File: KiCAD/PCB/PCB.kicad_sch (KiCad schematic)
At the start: 62 parts, among them J1 Conn_01x04, J2 Conn_01x02, P1 USB_C_Plug, Q1 Q_NPN_EBC, Q2 Q_NPN_EBC, SW1 SW_Push, SW2 SW_Push, SW3 RotaryEncoder_Switch, SW4 SW_Push, SW5 SW_Push, U1 MIC5219-3.3YM5, U2 CH340G, U3 MCP73832-5-OT, U4 ESP32-WROOM-32D, U5 MPU-6050, Y1 12Mhz

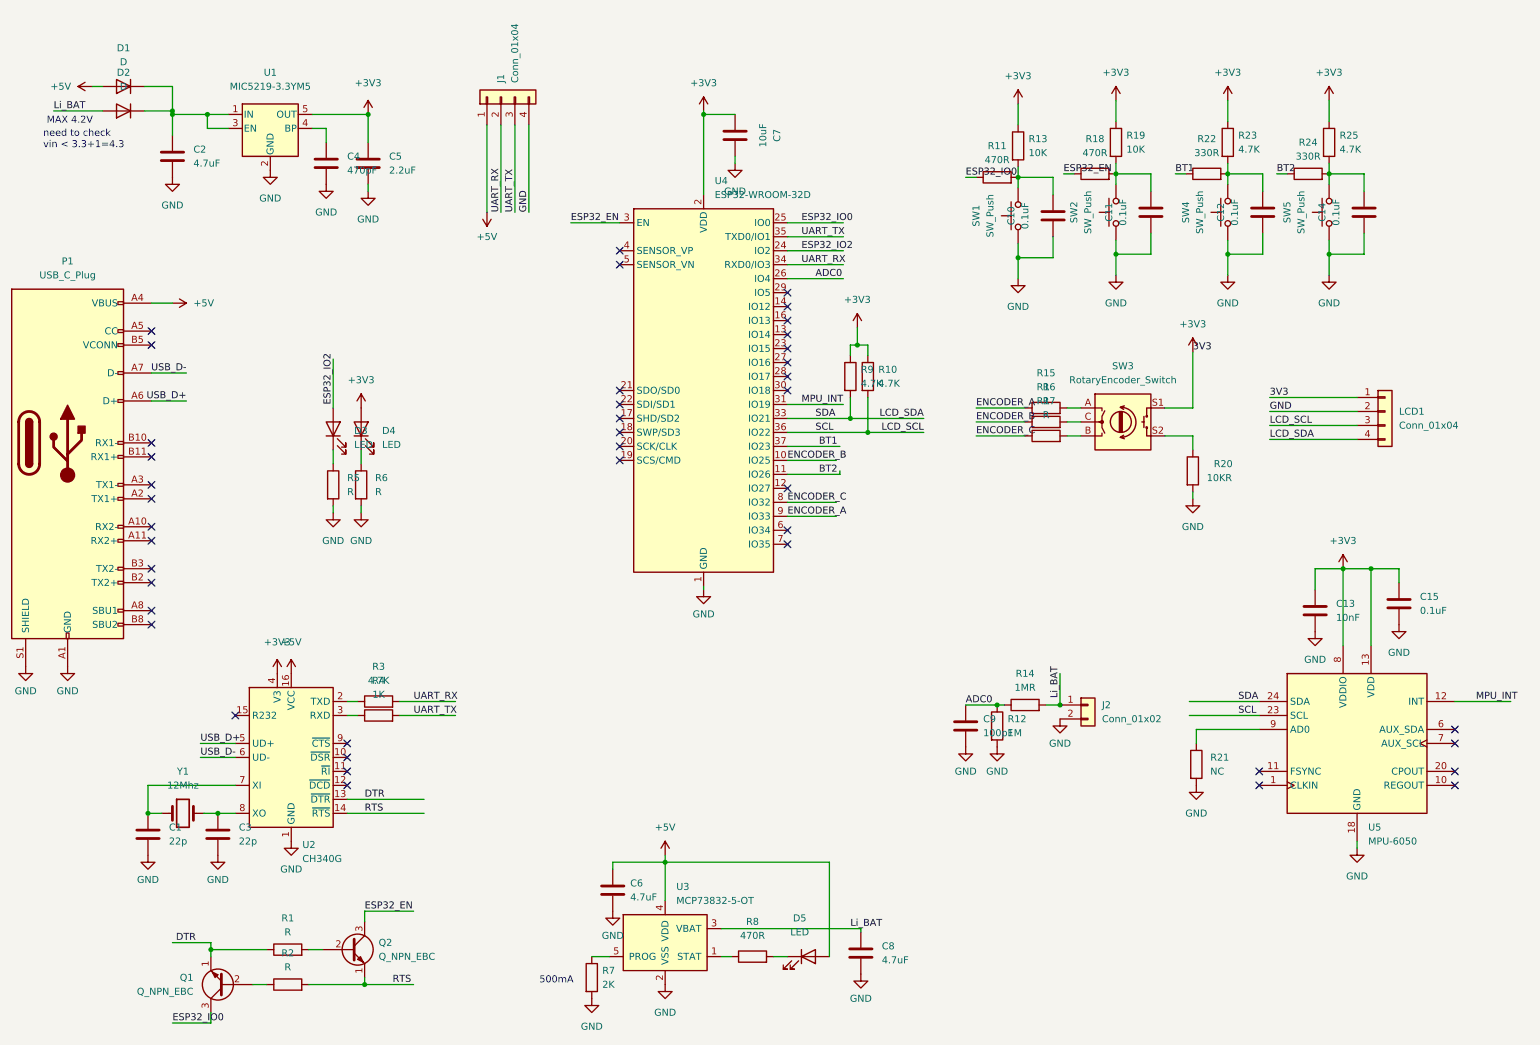
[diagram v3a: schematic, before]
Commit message: 更新第二版原理圖
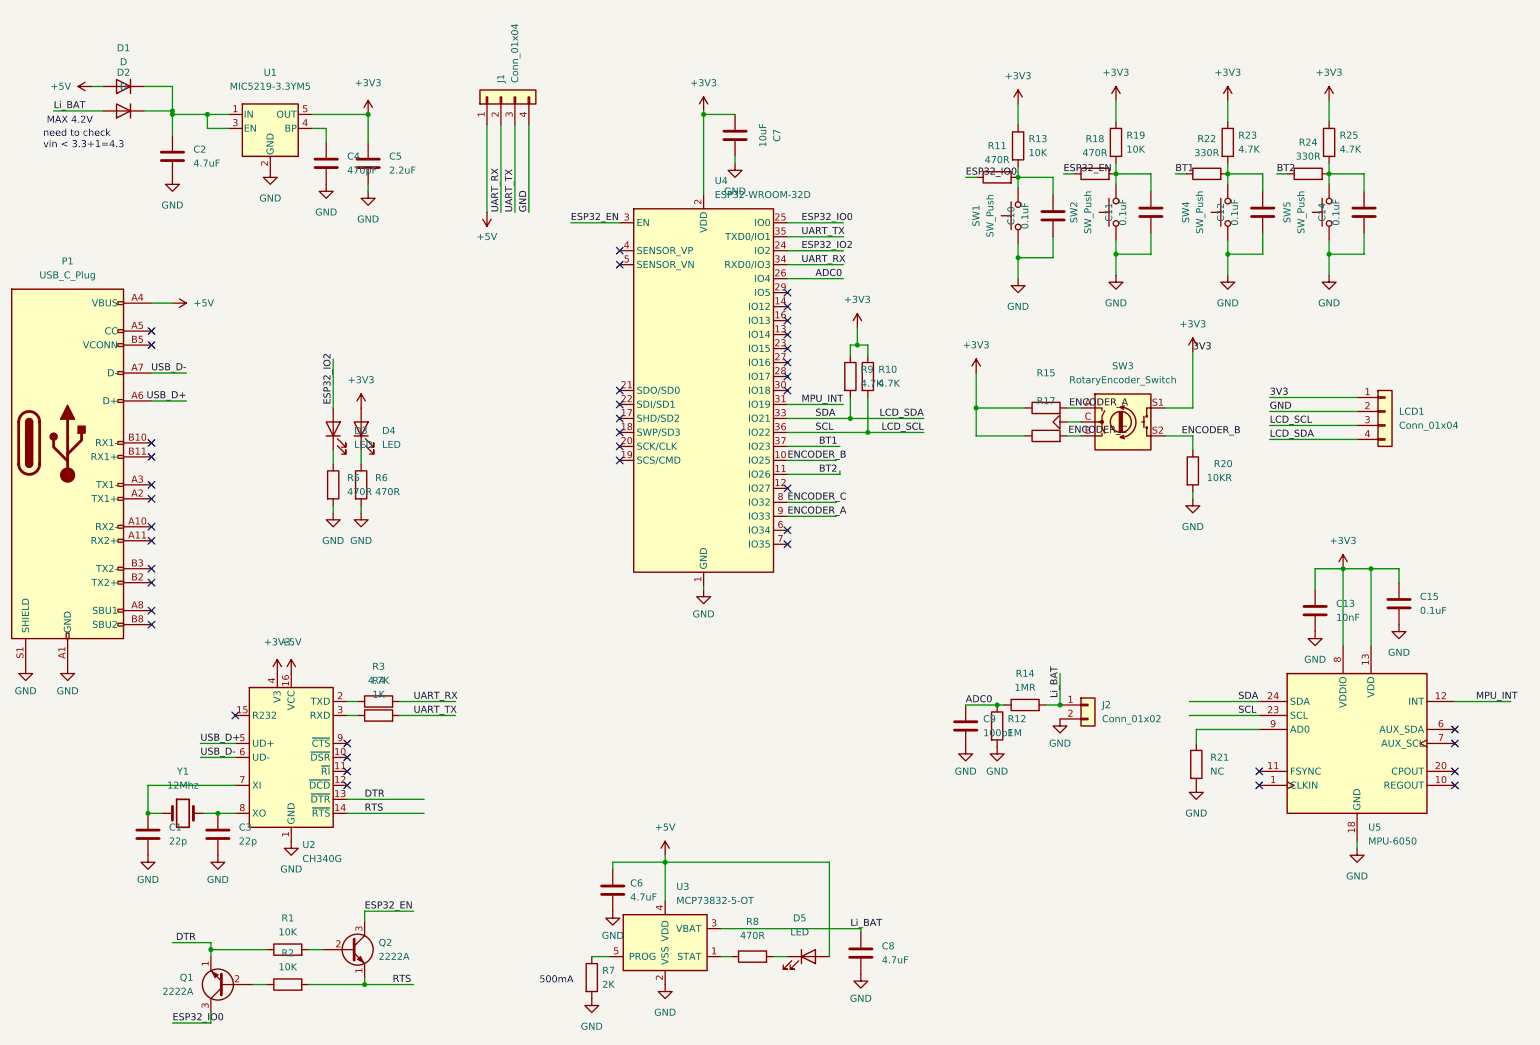
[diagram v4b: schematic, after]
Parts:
- removed R16: R, Resistor_SMD:R_0402_1005Metric, symbol Device:R
- Q1, Q2: value Q_NPN_EBC -> 2222A
- R1, R2: value R -> 10K
- R15, R17: value R -> (none); footprint Resistor_SMD:R_0402_1005Metric -> (none)
- R5, R6: value R -> 470R
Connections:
- net +3V3: now also R15.1, R17.1
- net ENCODER_A: no longer R15.1
- net ENCODER_B: now also R20.1, SW3.S2
- net ENCODER_C: no longer R17.1
- net GND: now also SW3.C
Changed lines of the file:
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@@
   (junction (at 79.375 24.765) (diameter 0) (color 0 0 0 0)
+  )
+  (junction (at 189.865 78.105) (diameter 0) (color 0 0 0 0)
   )
   (junction (at 197.485 50.8) (diameter 0) (color 0 0 0 0)
@@
     (stroke (width 0) (type default) (color 0 0 0 0))
   )
+  (wire (pts (xy 189.865 78.105) (xy 189.865 83.185))
+    (stroke (width 0) (type default) (color 0 0 0 0))
+  )
   (wire (pts (xy 229.235 83.185) (xy 229.235 85.725))
     (stroke (width 0) (type default) (color 0 0 0 0))
@@
     (stroke (width 0) (type default) (color 0 0 0 0))
   )
-  (wire (pts (xy 189.865 80.645) (xy 198.755 80.645))
-    (stroke (width 0) (type default) (color 0 0 0 0))
-  )
   (wire (pts (xy 170.18 82.55) (xy 180.34 82.55))
     (stroke (width 0) (type default) (color 0 0 0 0))
@@
   )
   (wire (pts (xy 103.505 42.545) (xy 103.505 26.67))
+    (stroke (width 0) (type default) (color 0 0 0 0))
+  )
+  (wire (pts (xy 189.865 71.755) (xy 189.865 78.105))
     (stroke (width 0) (type default) (color 0 0 0 0))
   )
@@
     (effects (font (size 1.27 1.27)) (justify left bottom))
   )
-  (label "ENCODER_C" (at 189.865 83.185 0)
+  (label "ENCODER_C" (at 206.6036 83.1088 0)
     (effects (font (size 1.27 1.27)) (justify left bottom))
   )
@@
     (effects (font (size 1.27 1.27)) (justify left bottom))
   )
-  (label "ENCODER_A" (at 189.865 78.105 0)
+  (label "ENCODER_A" (at 206.756 78.1304 0)
     (effects (font (size 1.27 1.27)) (justify left bottom))
   )
@@
     (effects (font (size 1.27 1.27)) (justify left bottom))
   )
-  (label "ENCODER_B" (at 189.865 80.645 0)
+  (label "ENCODER_B" (at 227.203 83.185 0)
     (effects (font (size 1.27 1.27)) (justify left bottom))
   )
@@
       (effects (font (size 1.27 1.27)) (justify left))
     )
-    (property "Value" "R" (id 1) (at 80.645 93.3449 0)
+    (property "Value" "470R" (id 1) (at 80.645 93.3449 0)
       (effects (font (size 1.27 1.27)) (justify left))
     )
@@
       (effects (font (size 1.27 1.27)) (justify left))
     )
-    (property "Value" "R" (id 1) (at 75.565 93.3449 0)
+    (property "Value" "470R" (id 1) (at 75.565 93.3449 0)
       (effects (font (size 1.27 1.27)) (justify left))
     )
@@
       (effects (font (size 1.27 1.27)) (justify left))
     )
-    (property "Value" "Q_NPN_EBC" (id 1) (at 81.28 177.7999 0)
+    (property "Value" "2222A" (id 1) (at 81.28 177.7999 0)
       (effects (font (size 1.27 1.27)) (justify left))
     )
@@
     (in_bom yes) (on_board yes) (fields_autoplaced)
     (property "Reference" "R2" (id 0) (at 64.77 177.165 90))
-    (property "Value" "R" (id 1) (at 64.77 179.705 90))
+    (property "Value" "10K" (id 1) (at 64.77 179.705 90))
     (property "Footprint" "Resistor_SMD:R_0402_1005Metric" (id 2) (at 64.77 184.658 90)
       (effects (font (size 1.27 1.27)) hide)
@@
       (effects (font (size 1.27 1.27)) (justify left))
     )
-    (property "Value" "Q_NPN_EBC" (id 1) (at 47.625 184.1499 0)
+    (property "Value" "2222A" (id 1) (at 47.625 184.1499 0)
       (effects (font (size 1.27 1.27)) (justify left))
     )
@@
     (in_bom yes) (on_board yes) (fields_autoplaced)
     (property "Reference" "R15" (id 0) (at 202.565 71.755 90))
-    (property "Value" "R" (id 1) (at 202.565 74.295 90))
-    (property "Footprint" "Resistor_SMD:R_0402_1005Metric" (id 2) (at 202.565 79.883 90)
+    (property "Value" "" (id 1) (at 202.565 74.295 90))
+    (property "Footprint" "" (id 2) (at 202.565 79.883 90)
       (effects (font (size 1.27 1.27)) hide)
     )
@@
     (pin "1")
   )
+  (symbol (lib_id "power:GND") (at 206.375 80.645 270) (unit 1)
+    (in_bom yes) (on_board yes) (fields_autoplaced)
+    (property "Reference" "#PWR?" (id 0) (at 200.025 80.645 0)
+      (effects (font (size 1.27 1.27)) hide)
+    )
+    (property "Value" "" (id 1) (at 203.2 80.6449 90)
+      (effects (font (size 1.27 1.27)) (justify right))
+    )
+    (property "Footprint" "" (id 2) (at 206.375 80.645 0)
+      (effects (font (size 1.27 1.27)) hide)
+    )
+    (property "Datasheet" "" (id 3) (at 206.375 80.645 0)
+      (effects (font (size 1.27 1.27)) hide)
+    )
+    (pin "1")
+  )
   (symbol (lib_id "Device:R") (at 254 29.845 0) (unit 1)
     (in_bom yes) (on_board yes) (fields_autoplaced)
@@
     (pin "S2")
   )
-  (symbol (lib_id "Device:R") (at 202.565 80.645 90) (unit 1)
-    (in_bom yes) (on_board yes) (fields_autoplaced)
-    (property "Reference" "R16" (id 0) (at 202.565 74.295 90))
-    (property "Value" "R" (id 1) (at 202.565 76.835 90))
-    (property "Footprint" "Resistor_SMD:R_0402_1005Metric" (id 2) (at 202.565 82.423 90)
-      (effects (font (size 1.27 1.27)) hide)
-    )
-    (property "Datasheet" "~" (id 3) (at 202.565 80.645 0)
-      (effects (font (size 1.27 1.27)) hide)
-    )
-    (pin "1")
-    (pin "2")
-  )
   (symbol (lib_id "Device:D") (at 34.925 19.685 180) (unit 1)
     (in_bom yes) (on_board yes) (fields_autoplaced)
@@
     (in_bom yes) (on_board yes) (fields_autoplaced)
     (property "Reference" "R17" (id 0) (at 202.565 76.835 90))
-    (property "Value" "R" (id 1) (at 202.565 79.375 90))
-    (property "Footprint" "Resistor_SMD:R_0402_1005Metric" (id 2) (at 202.565 84.963 90)
+    (property "Value" "" (id 1) (at 202.565 79.375 90))
+    (property "Footprint" "" (id 2) (at 202.565 84.963 90)
       (effects (font (size 1.27 1.27)) hide)
     )
@@
     (in_bom yes) (on_board yes) (fields_autoplaced)
     (property "Reference" "R1" (id 0) (at 64.77 170.815 90))
-    (property "Value" "R" (id 1) (at 64.77 173.355 90))
+    (property "Value" "10K" (id 1) (at 64.77 173.355 90))
     (property "Footprint" "Resistor_SMD:R_0402_1005Metric" (id 2) (at 64.77 178.308 90)
       (effects (font (size 1.27 1.27)) hide)
@@
     (pin "1")
     (pin "2")
+  )
+  (symbol (lib_id "power:+3V3") (at 189.865 71.755 0) (unit 1)
+    (in_bom yes) (on_board yes) (fields_autoplaced)
+    (property "Reference" "#PWR?" (id 0) (at 189.865 75.565 0)
+      (effects (font (size 1.27 1.27)) hide)
+    )
+    (property "Value" "+3V3" (id 1) (at 189.865 66.675 0))
+    (property "Footprint" "" (id 2) (at 189.865 71.755 0)
+      (effects (font (size 1.27 1.27)) hide)
+    )
+    (property "Datasheet" "" (id 3) (at 189.865 71.755 0)
+      (effects (font (size 1.27 1.27)) hide)
+    )
+    (pin "1")
   )
   (symbol (lib_id "Device:R") (at 120.015 181.61 0) (unit 1)
@@
       (reference "#PWR?") (unit 1) (value "+3V3") (footprint "")
     )
+    (path "/cf8412e7-e7b5-4c85-a32c-ec03401d775a"
+      (reference "#PWR?") (unit 1) (value "GND") (footprint "")
+    )
+    (path "/f72b6ed7-2481-4a09-9868-7d9138063f42"
+      (reference "#PWR?") (unit 1) (value "+3V3") (footprint "")
+    )
     (path "/0b9c0493-9597-4867-be8d-3f448f5ca7e5"
       (reference "C1") (unit 1) (value "22p") (footprint "Capacitor_SMD:C_0603_1608Metric")
@@
     )
     (path "/507a99e5-3d90-4793-9e5b-a136ac8962d2"
-      (reference "Q1") (unit 1) (value "Q_NPN_EBC") (footprint "Package_TO_SOT_SMD:SOT-23")
+      (reference "Q1") (unit 1) (value "2222A") (footprint "Package_TO_SOT_SMD:SOT-23")
     )
     (path "/2e074f0f-8257-41be-9cae-d8c8a2b908f8"
-      (reference "Q2") (unit 1) (value "Q_NPN_EBC") (footprint "Package_TO_SOT_SMD:SOT-23")
+      (reference "Q2") (unit 1) (value "2222A") (footprint "Package_TO_SOT_SMD:SOT-23")
     )
     (path "/f3a22bc4-6449-4941-bfe2-c6afaf618f51"
-      (reference "R1") (unit 1) (value "R") (footprint "Resistor_SMD:R_0402_1005Metric")
+      (reference "R1") (unit 1) (value "10K") (footprint "Resistor_SMD:R_0402_1005Metric")
     )
     (path "/4236cd41-26ae-4647-83a1-307f90216d9a"
-      (reference "R2") (unit 1) (value "R") (footprint "Resistor_SMD:R_0402_1005Metric")
+      (reference "R2") (unit 1) (value "10K") (footprint "Resistor_SMD:R_0402_1005Metric")
     )
     (path "/d2fc5f4a-aa81-48c8-8561-d4ee9491e7c3"
@@
     )
     (path "/196afe34-74fd-48ae-9b9f-d7a341cb4cdd"
-      (reference "R5") (unit 1) (value "R") (footprint "Resistor_SMD:R_0402_1005Metric")
+      (reference "R5") (unit 1) (value "470R") (footprint "Resistor_SMD:R_0402_1005Metric")
     )
     (path "/05551453-3a94-4924-93a1-3af33c189f3e"
-      (reference "R6") (unit 1) (value "R") (footprint "Resistor_SMD:R_0402_1005Metric")
+      (reference "R6") (unit 1) (value "470R") (footprint "Resistor_SMD:R_0402_1005Metric")
     )
     (path "/f74e1ca4-f78b-4973-afe1-7ee6552c2270"
@@
     )
     (path "/9419c83f-48f3-4f0c-8c63-024115c8cba6"
-      (reference "R15") (unit 1) (value "R") (footprint "Resistor_SMD:R_0402_1005Metric")
-    )
-    (path "/dd31eb64-1182-4c2c-9eeb-37f8591a9058"
-      (reference "R16") (unit 1) (value "R") (footprint "Resistor_SMD:R_0402_1005Metric")
+      (reference "R15") (unit 1) (value "10KR") (footprint "Resistor_SMD:R_0402_1005Metric")
     )
     (path "/f1c16499-a02d-4e91-9bd7-b072bba69005"
-      (reference "R17") (unit 1) (value "R") (footprint "Resistor_SMD:R_0402_1005Metric")
+      (reference "R17") (unit 1) (value "10KR") (footprint "Resistor_SMD:R_0402_1005Metric")
     )
     (path "/e96445b3-f69a-47ec-ae68-fee1f1a58c81"
